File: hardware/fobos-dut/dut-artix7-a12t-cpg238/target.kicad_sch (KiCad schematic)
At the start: 41 parts

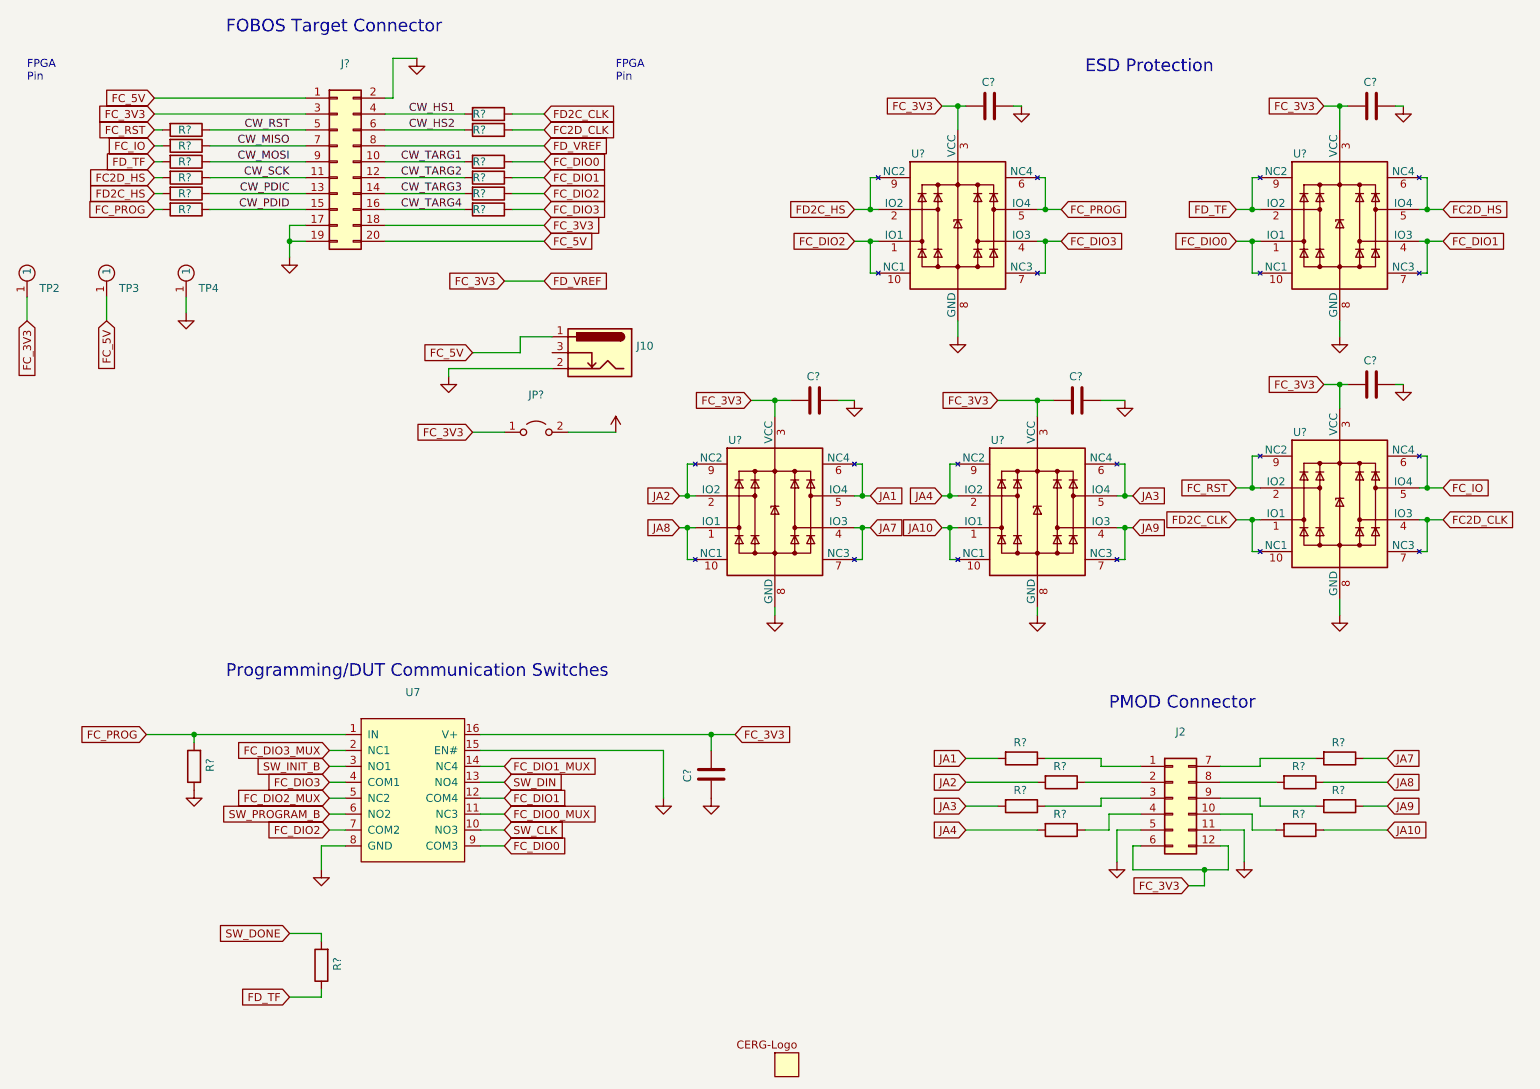
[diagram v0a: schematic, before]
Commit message: transitioned artix-7 dut to Kikad 6
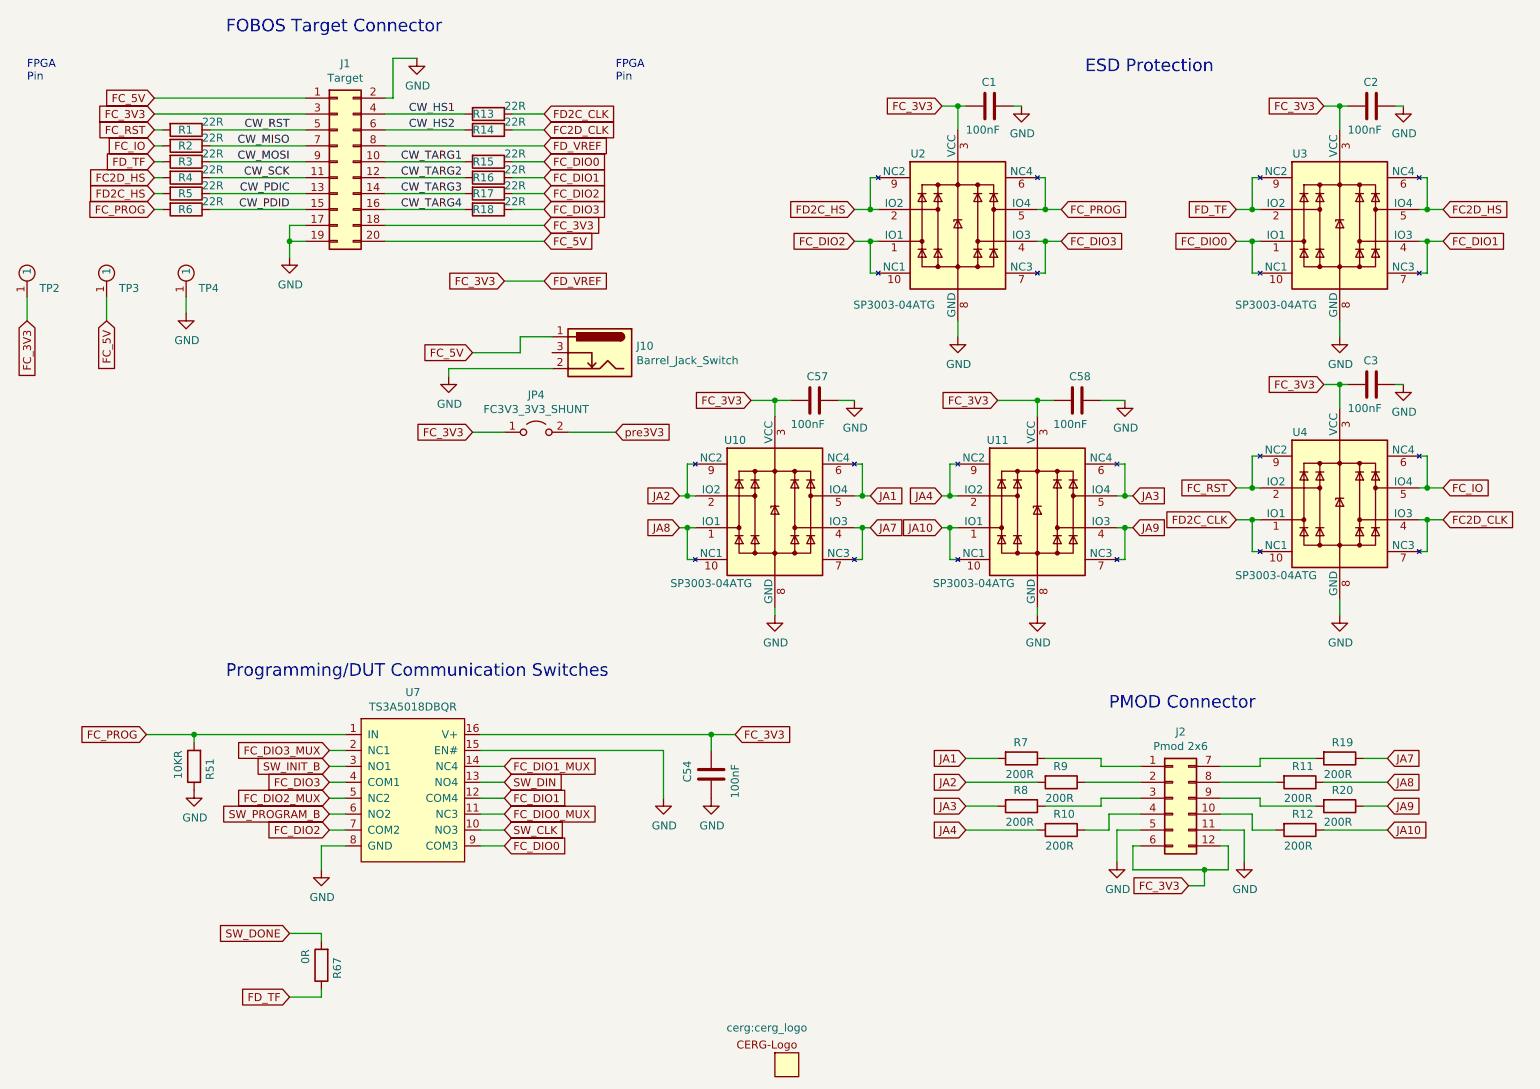
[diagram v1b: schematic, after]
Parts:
- C1, C2, C3, C54, C57, C58: renamed from C?; value (none) -> 100nF; footprint (none) -> Capacitor_SMD:C_0603_1608Metric
- J1: renamed from J?; value (none) -> Target; footprint (none) -> Connector_IDC:IDC-Header_2x10_P2.54mm_Horizontal
- J10: value (none) -> Barrel_Jack_Switch; footprint (none) -> cerg:BarrelJack_CUI_PJ-102AH_Horizontal
- J2: value (none) -> Pmod 2x6; footprint (none) -> fobos-shield:PinSocket_2x06_P2.54mm_Horizontal_FLipped
- JP4: renamed from JP?; value (none) -> FC3V3_3V3_SHUNT; footprint (none) -> Connector_PinHeader_2.54mm:PinHeader_1x02_P2.54mm_Vertical
- R1, R13, R14, R15, R16, R17, R18, R2, R3, R4, R5, R6: renamed from R?; value (none) -> 22R; footprint (none) -> Resistor_SMD:R_0603_1608Metric
- R10, R11, R12, R19, R20, R7, R8, R9: renamed from R?; value (none) -> 200R; footprint (none) -> Resistor_SMD:R_0603_1608Metric
- R51: renamed from R?; value (none) -> 10KR; footprint (none) -> Resistor_SMD:R_0603_1608Metric
- R67: renamed from R?; value (none) -> 0R; footprint (none) -> Resistor_SMD:R_0603_1608Metric
- TP2, TP3, TP4: value (none) -> 5281; footprint (none) -> cerg:5281
- U10, U11, U2, U3, U4: renamed from U?; value (none) -> SP3003-04ATG; footprint (none) -> Package_SO:MSOP-10_3x3mm_P0.5mm
- U7: value (none) -> TS3A5018DBQR; footprint (none) -> cerg:SSOP-16_4.0x5.0mm_P0.635mm
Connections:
- net +3V3 renamed pre3V3
